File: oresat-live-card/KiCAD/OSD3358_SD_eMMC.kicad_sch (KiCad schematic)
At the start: 31 parts, among them J7 DM3BT-DSF-PEJS, U11 TCAN330, U3 EMMC+RESET+5.1-COMPATIBLE-BA, U7 OSD3358-512M-BSM

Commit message: Updated OreSat Live Card. Added changes from the C3 v6 Octavo circuitry and GPS card update. Fixed some GitHub issues. Board layout still in progress.
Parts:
- added R97: 0, Resistor_SMD:R_0603_1608Metric, symbol oresat-passives:R-US
- D2, D3, D4, D5: symbol oresat-live-card-eagle-import:LED-BLUE0603 -> Device:LED
- J7: symbol oresat-live-card-eagle-import:DM3BT-DSF-PEJS -> oresat-connectors:DM3BT-DSF-PEJS
- R10, R8, R9: symbol oresat-live-card-eagle-import:EXB-A10P391JC_ARRAY_EXBA-M -> oresat-passives:EXB-A10P391J
- R2, R3, R4, R5: symbol oresat-live-card-eagle-import:R-US_0603-A -> oresat-passives:R-US
- TP142, TP146, TP177, TP178, TP22, TP35: footprint oresat-live-card:PAD.03X.04 -> oresat-misc:TestPoint_Pad_D1.0mm; symbol oresat-live-card-eagle-import:TEST-POINT -> oresat-misc:Test-Point-1mm-round
- U11: symbol oresat-live-card-eagle-import:TCAN330 -> oresat-ics:TCAN330
- U3: footprint oresat-live-card:BGA-153(11.5X13)(EMMC-BA) -> oresat-ics:BGA-153(11.5X13)(EMMC-BA); symbol oresat-live-card-eagle-import:EMMC+RESET+5.1-COMPATIBLE-BA -> oresat-ics:EMMC+RESET+5.1-COMPATIBLE-BA
- U7: footprint oresat-live-card:OSD335X-BGA-256 -> oresat-ics:U-Octavo-OSD335X-BGA-256; symbol oresat-live-card-eagle-import:OSD3358-512M-BSM -> oresat-ics:OSD3358-512M-BSM
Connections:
- net 3.3V: now also R97.2; no longer C2.1, C5.1, C6.1, C78.1, C9.1, U3.C6 (VDDQ), U3.E6 (VDDIO), U3.F5 (VDDIO), U3.J10 (VDDIO), U3.K9 (VDDIO), U3.M4 (VDDQ), U3.N4 (VDDQ), U3.P3 (VDDQ), U3.P5 (VDDQ)
- net GND: now also D2.1 (K), D3.1 (K), D4.1 (K), D5.1 (K), U3.B11 (NC), U3.B14 (NC); no longer D2.C, D3.C, D4.C, D5.C
- net at R3.2: now also D3.2 (A); no longer D3.A
- net at R5.2: now also D5.2 (A); no longer D5.A
- net at R2.2: now also D2.2 (A); no longer D2.A
- net at R4.2: now also D4.2 (A); no longer D4.A
- new net: C2.1, C5.1, C6.1, C78.1, C9.1, R97.1, U3.B9 (NC), U3.C6 (VDDQ), U3.E6 (VDDIO), U3.F5 (VDDIO), U3.J10 (VDDIO), U3.K9 (VDDIO), U3.M4 (VDDQ), U3.N4 (VDDQ), U3.P3 (VDDQ), U3.P5 (VDDQ)
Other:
- moved on the sheet: C10, C11, C12, C2, C31, C5, C6, C78, C8, C9, J7, R10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

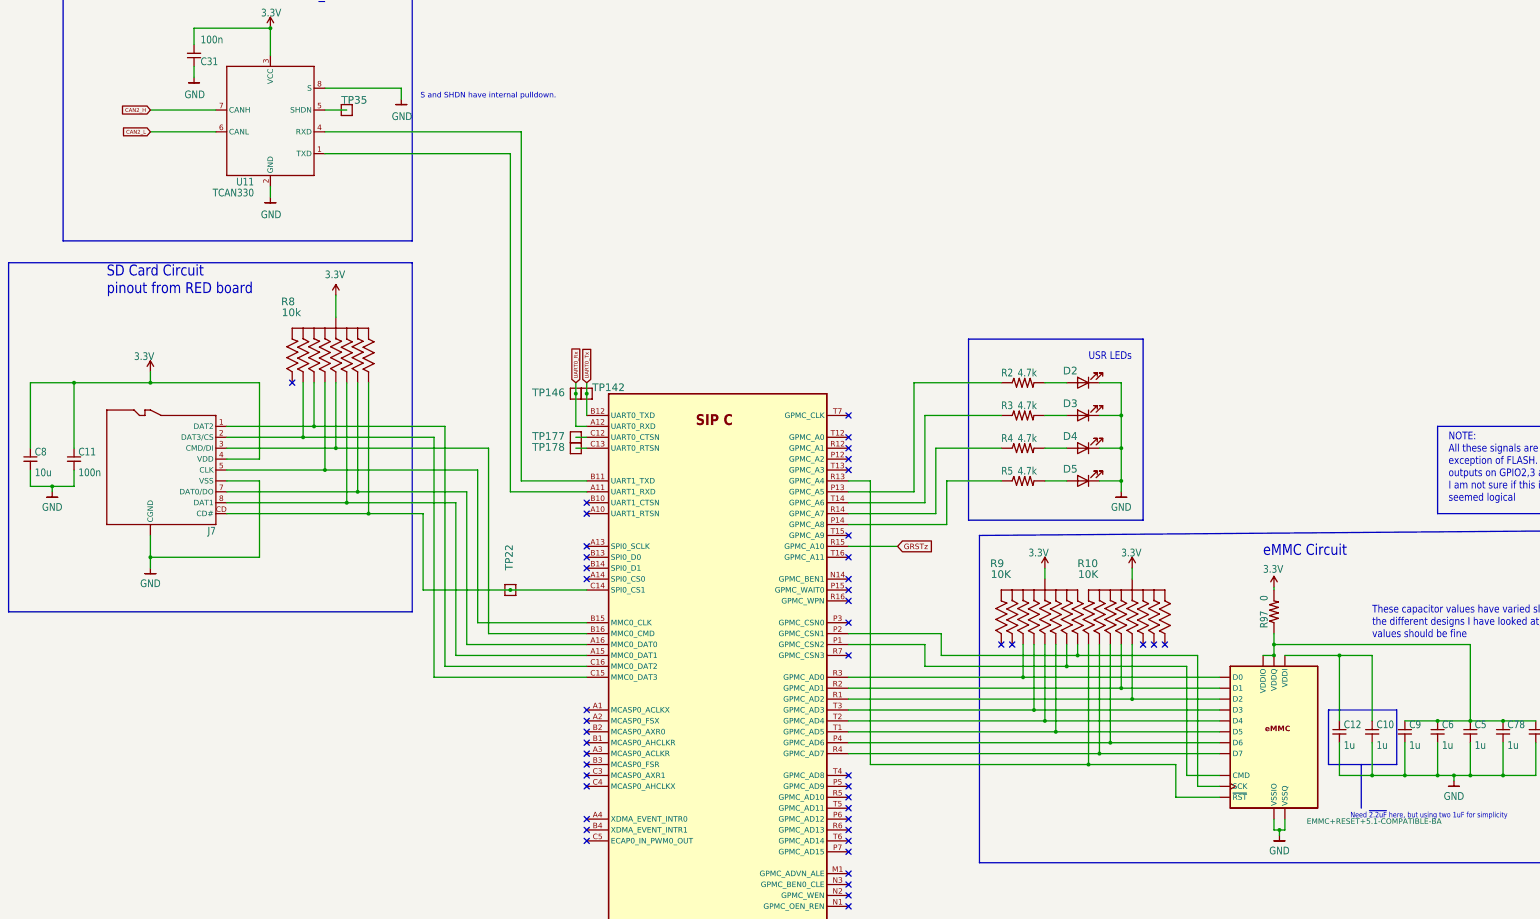
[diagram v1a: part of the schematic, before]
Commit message: Cleaned up ERC and DRC errors on DxWiFi Card
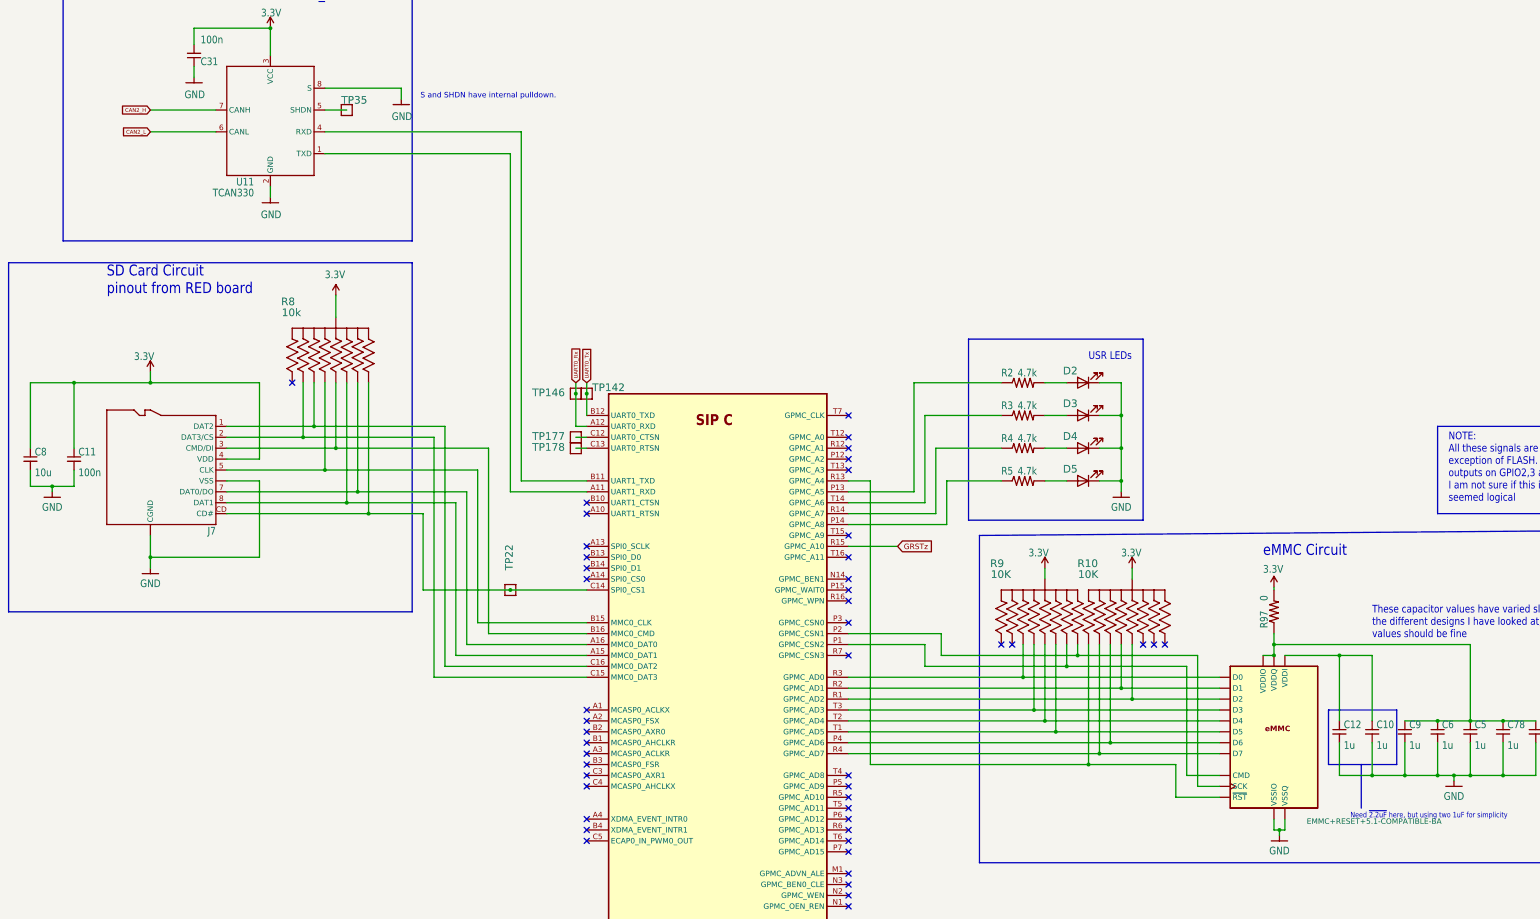
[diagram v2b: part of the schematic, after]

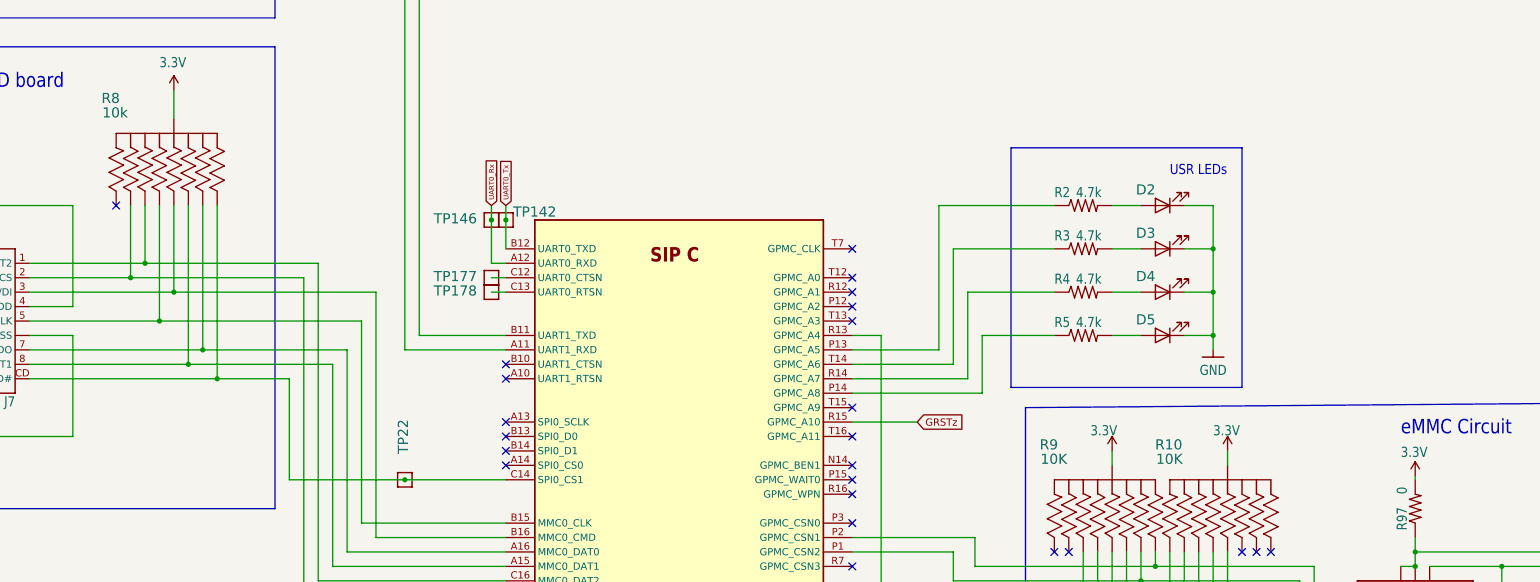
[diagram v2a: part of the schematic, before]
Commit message: Upgraded to KiCAD 8.0. Added notes on U.FL cable and USB cables to wifi and camera.
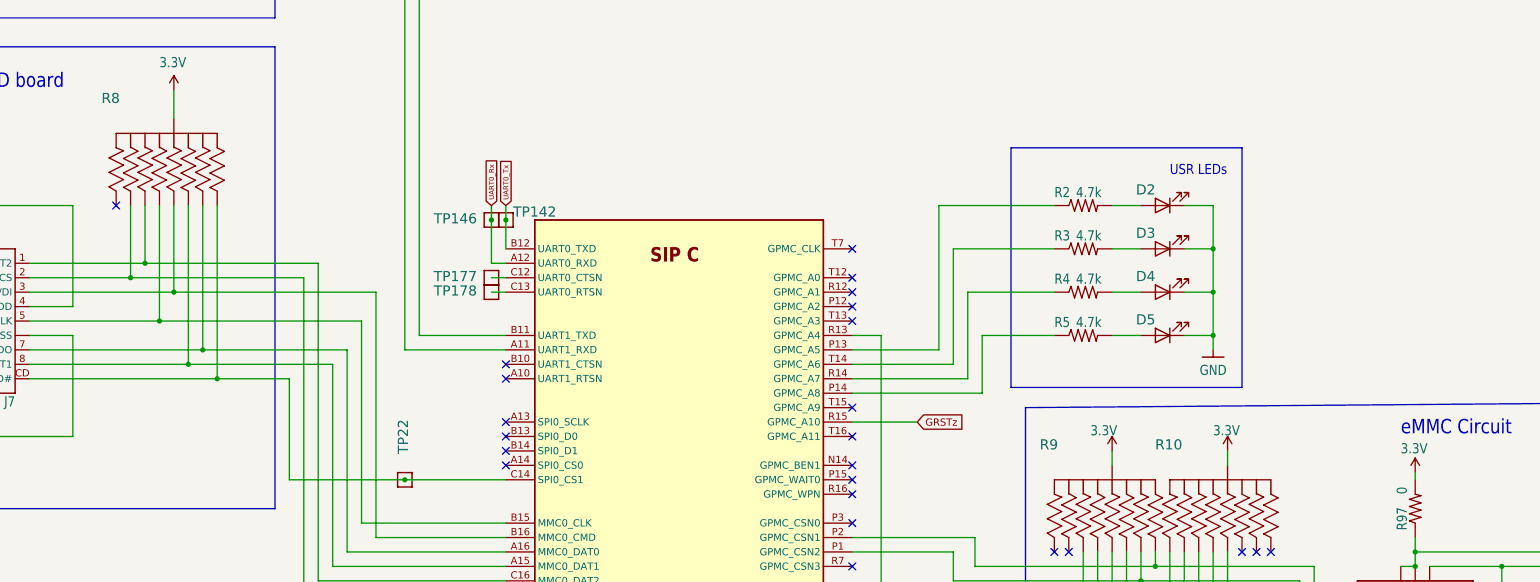
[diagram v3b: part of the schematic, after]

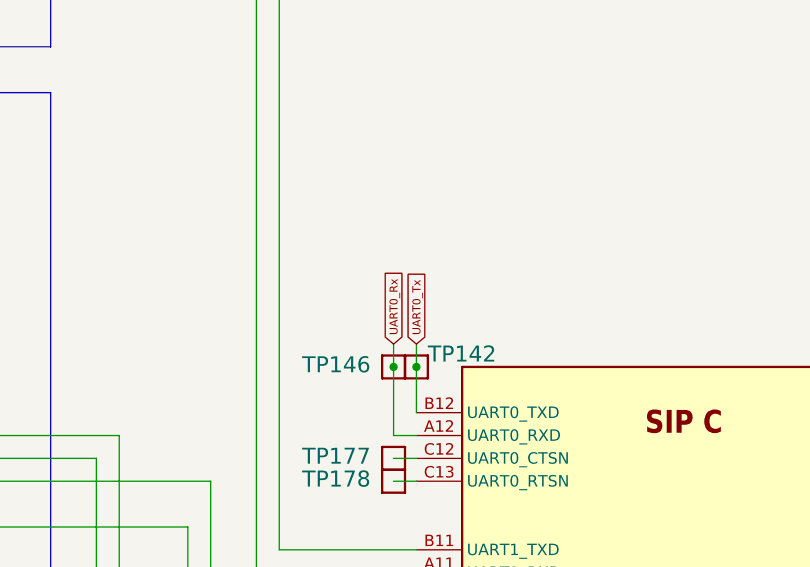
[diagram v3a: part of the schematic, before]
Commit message: added new sheets for LNA and switching
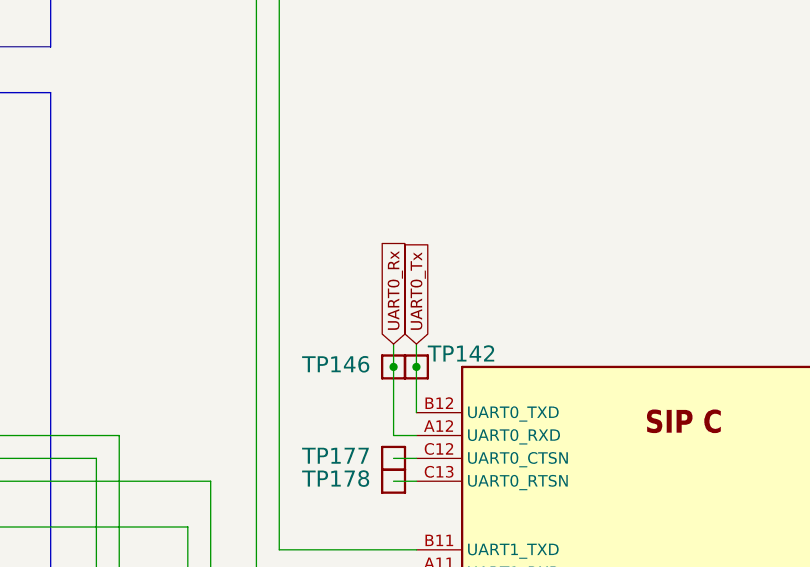
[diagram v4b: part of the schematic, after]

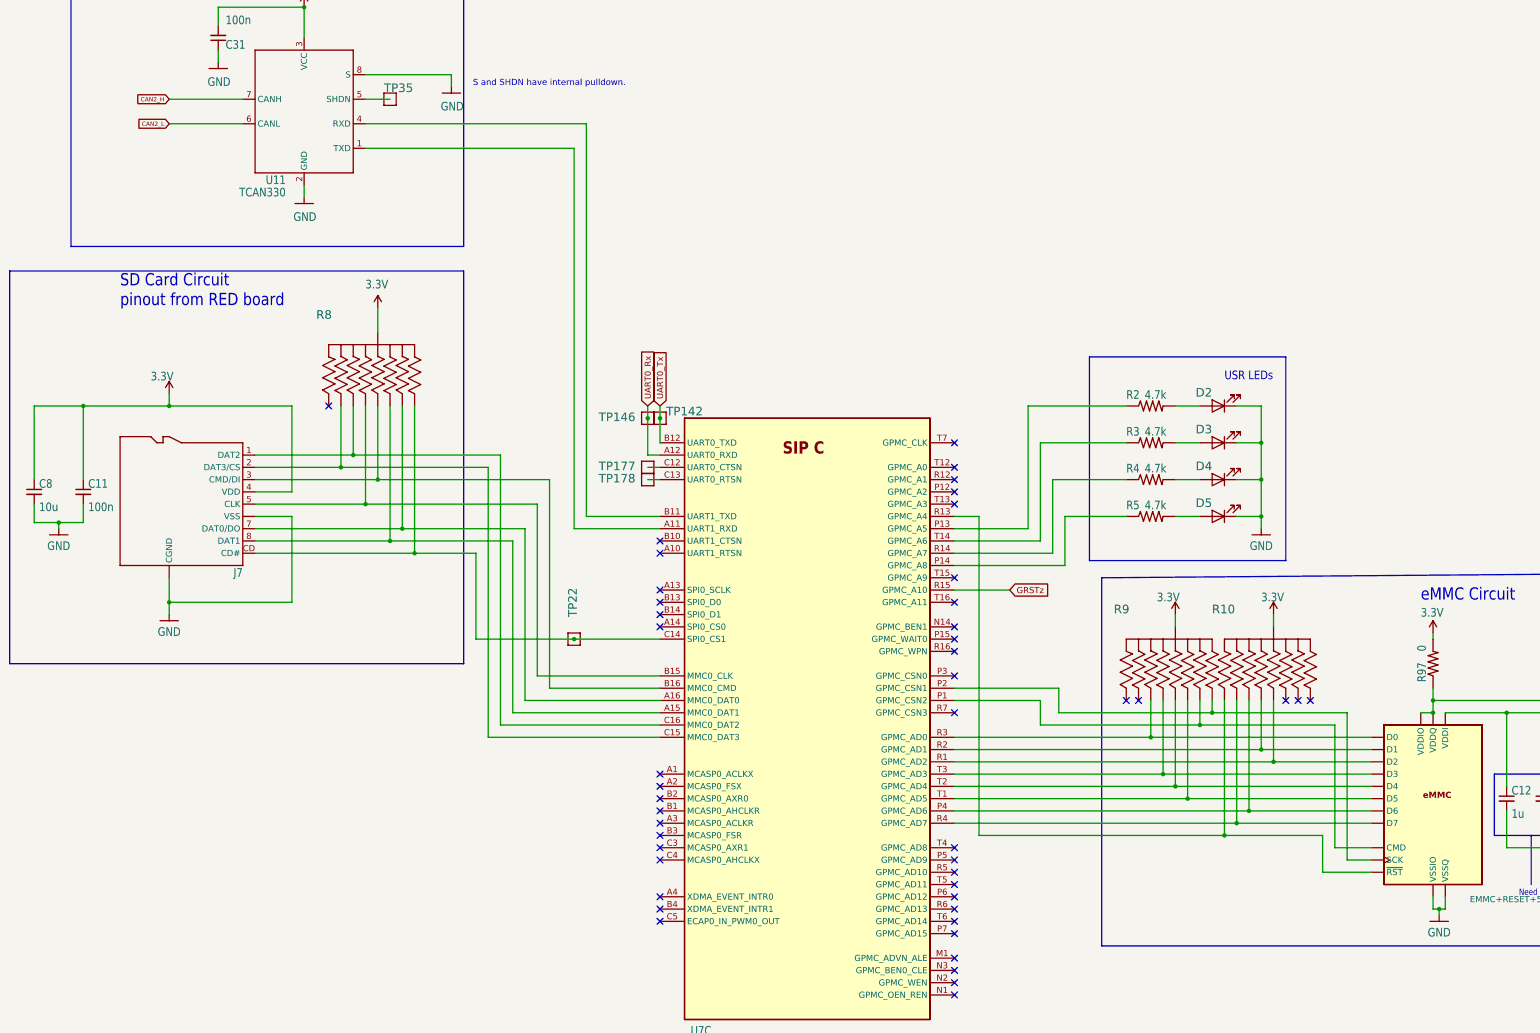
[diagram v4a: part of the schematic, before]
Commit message: completed tx/rx switch circuit and cleaned up GND references
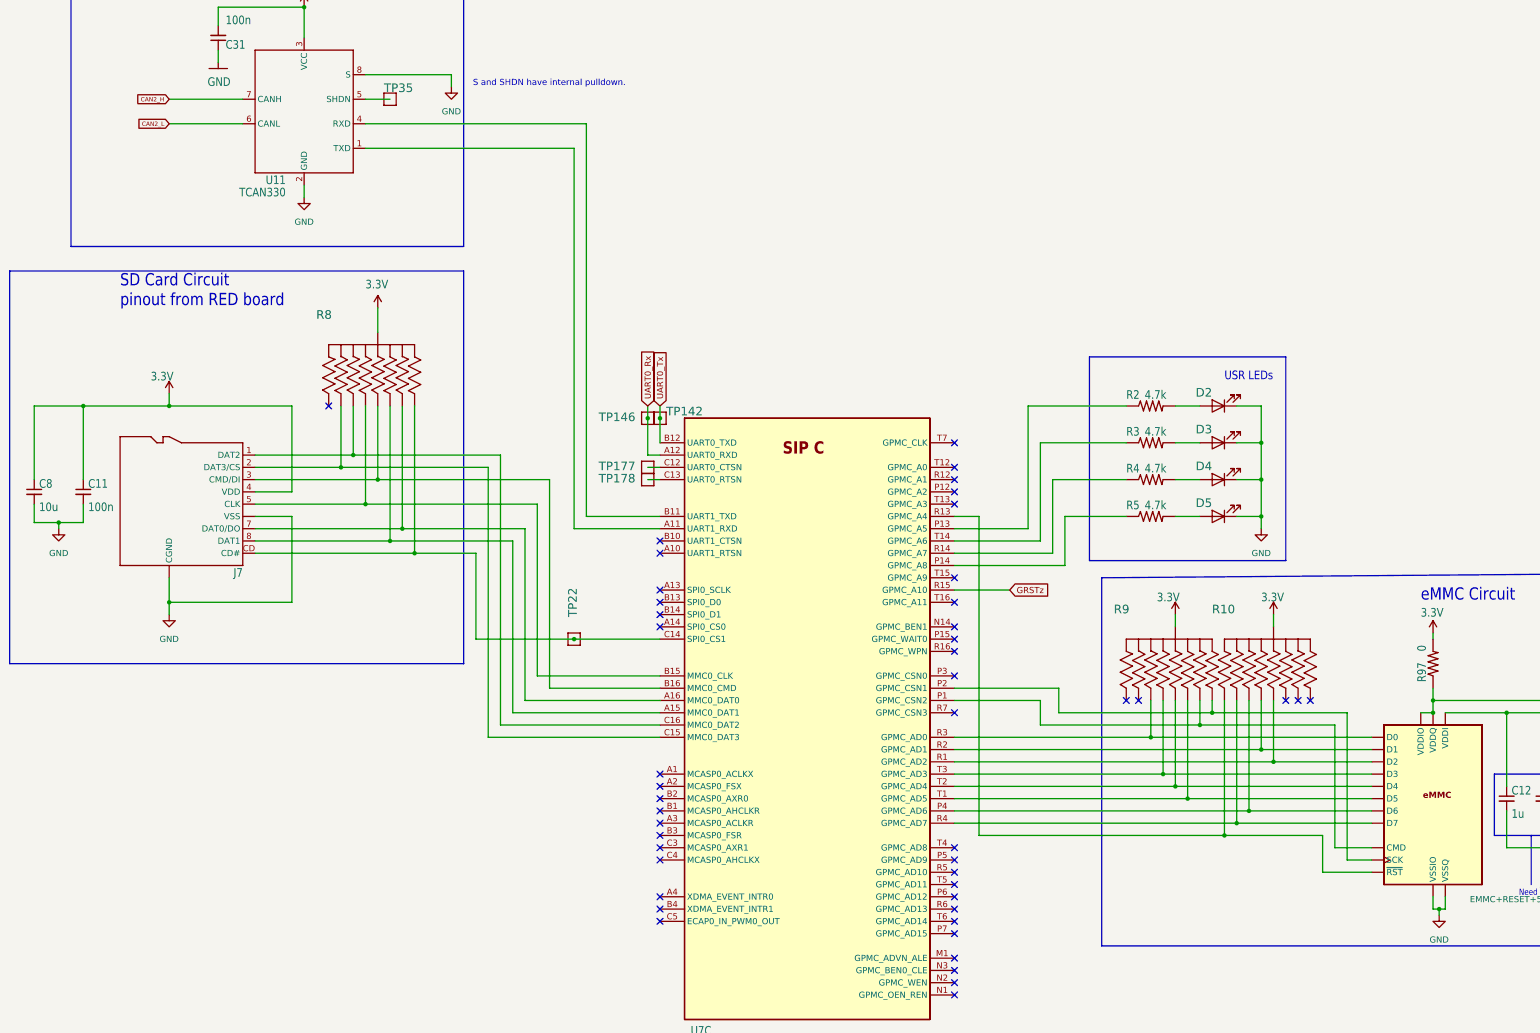
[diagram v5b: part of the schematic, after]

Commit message: Fixed up schematic as best as possible. There were a lot of issues with local paths being referenced, and EAGLE import libraries. Fixed all of those, as well as fixed some oresat-kicad IC symbols (bad direction pins) and I think we're now OK. Also updated card outline for two RF (LEFT) connectors.  Still missing two packages, but we'll deal with that later.
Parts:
- C10, C12, C5, C6, C78, C9: DPN (none) -> 445-12539-1-ND; MFR (none) -> TDK Corporation; MPN CGA3E1X7R1E105M080AE -> CGA3E1X7R1C105K080AC
- C11, C31: DPN (none) -> 445-5667-1-ND; MFR (none) -> TDK Corporation; MPN CL10B104KB8WPNC -> CGA3E2X7R1E104K080AA
- C2, C8: DPN (none) -> 445-16111-1-ND; MFR (none) -> TDK Corporation; MPN CGA4J1X7R0J106M125AC -> CGA4J1X7S1C106M125AC
- D2, D3, D4, D5: DPN (none) -> 732-150060BS75020CT-ND; MFR (none) -> Würth Elektronik
- J7: DPN (none) -> HR1942CT-ND; MFR (none) -> Hirose Electric Co Ltd
- R10, R9: value EXB-A10P103J -> 10k; DPN (none) -> U7103CT-ND; MFR (none) -> Panasonic
- R2, R3, R4, R5: DPN (none) -> ERJ-3EKF4701V; MFR (none) -> Panasonic
- R8: DPN (none) -> U7103CT-ND; MFR (none) -> Panasonic
- R97: DPN (none) -> P0.0GCT-ND; MFR (none) -> Panasonic; MPN ERJ-3EKF4701V -> ERJ-3GEY0R00V
- U11: value TCAN330 -> TCAN330G; DPN (none) -> 296-TCAN330GDCNRCT-ND; MFR (none) -> Texas Instruments; MPN TCAN330GDCN -> TCAN330GDCNR
- U3: value EMMC+RESET+5.1-COMPATIBLE-BA -> THGBMJG7C2LBAU8; DPN (none) -> 757-THGBMJG7C2LBAU8; Distributor DigiKey -> Mouser; MFR (none) -> Kioxia
- U7: DPN (none) -> 1676-1002-ND; MFR (none) -> Octavo Systems
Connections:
- net GND: no longer U3.B11 (NC), U3.B14 (NC)
- net at C2.1, C5.1, C6.1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: no longer U3.B9 (NC)
- net 3.3V renamed +3.3V
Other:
- moved on the sheet: C10, C12, C2, C5, C6, C78, C9, D2, D3, D4, D5, R2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
